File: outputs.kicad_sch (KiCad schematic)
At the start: 28 parts, among them J5 LED0123, J7 3.3V, M1 Motor_DC, U10 DRV2605LDGS, U21 WM8960, U9 PLP5012PWR

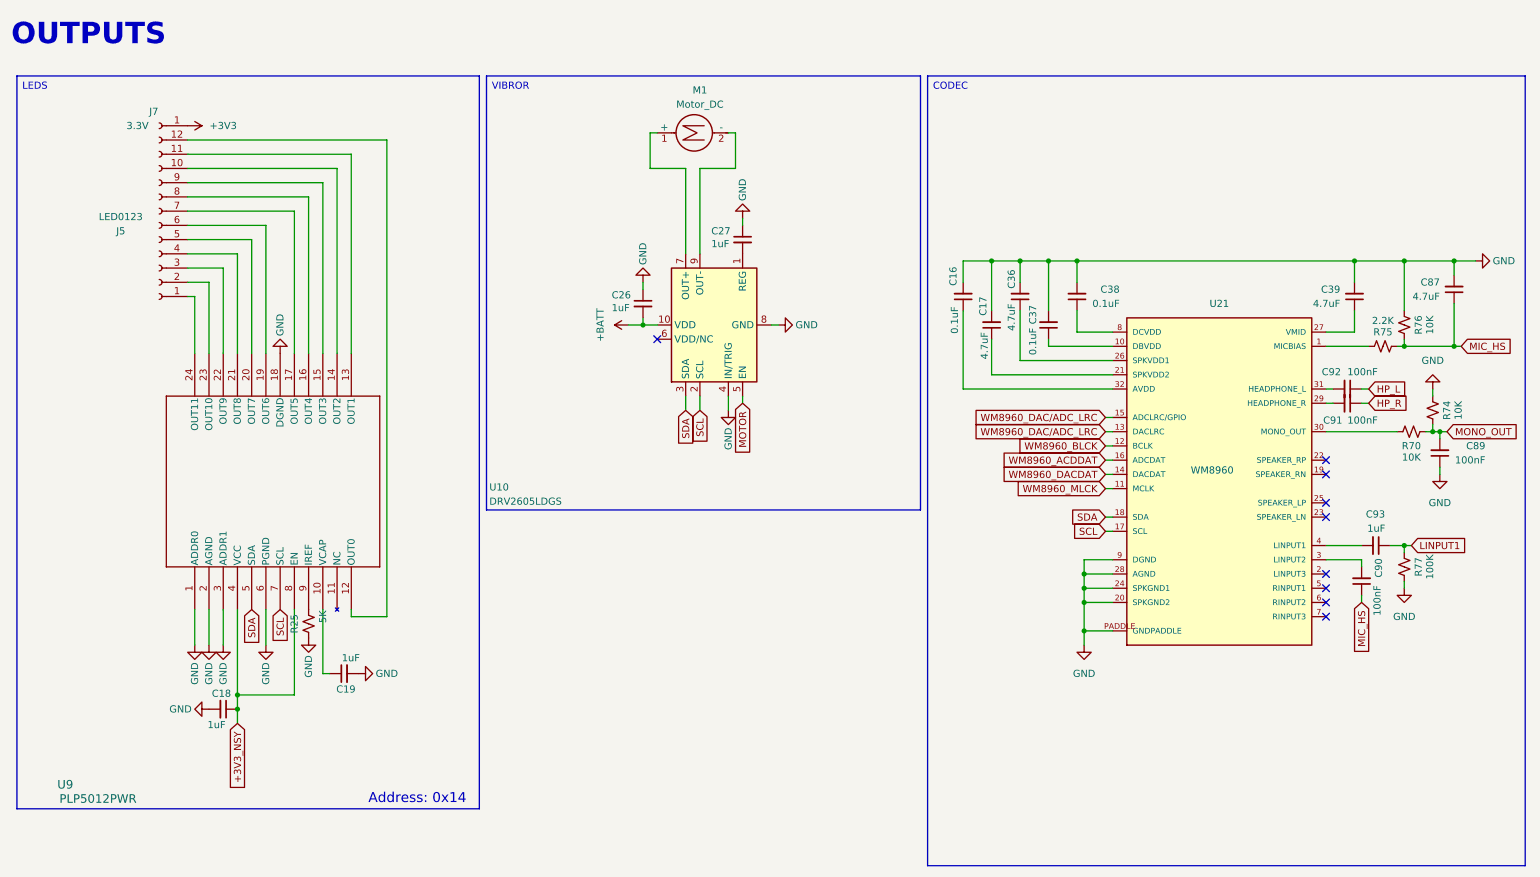
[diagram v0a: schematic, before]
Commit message: Routed RF Core
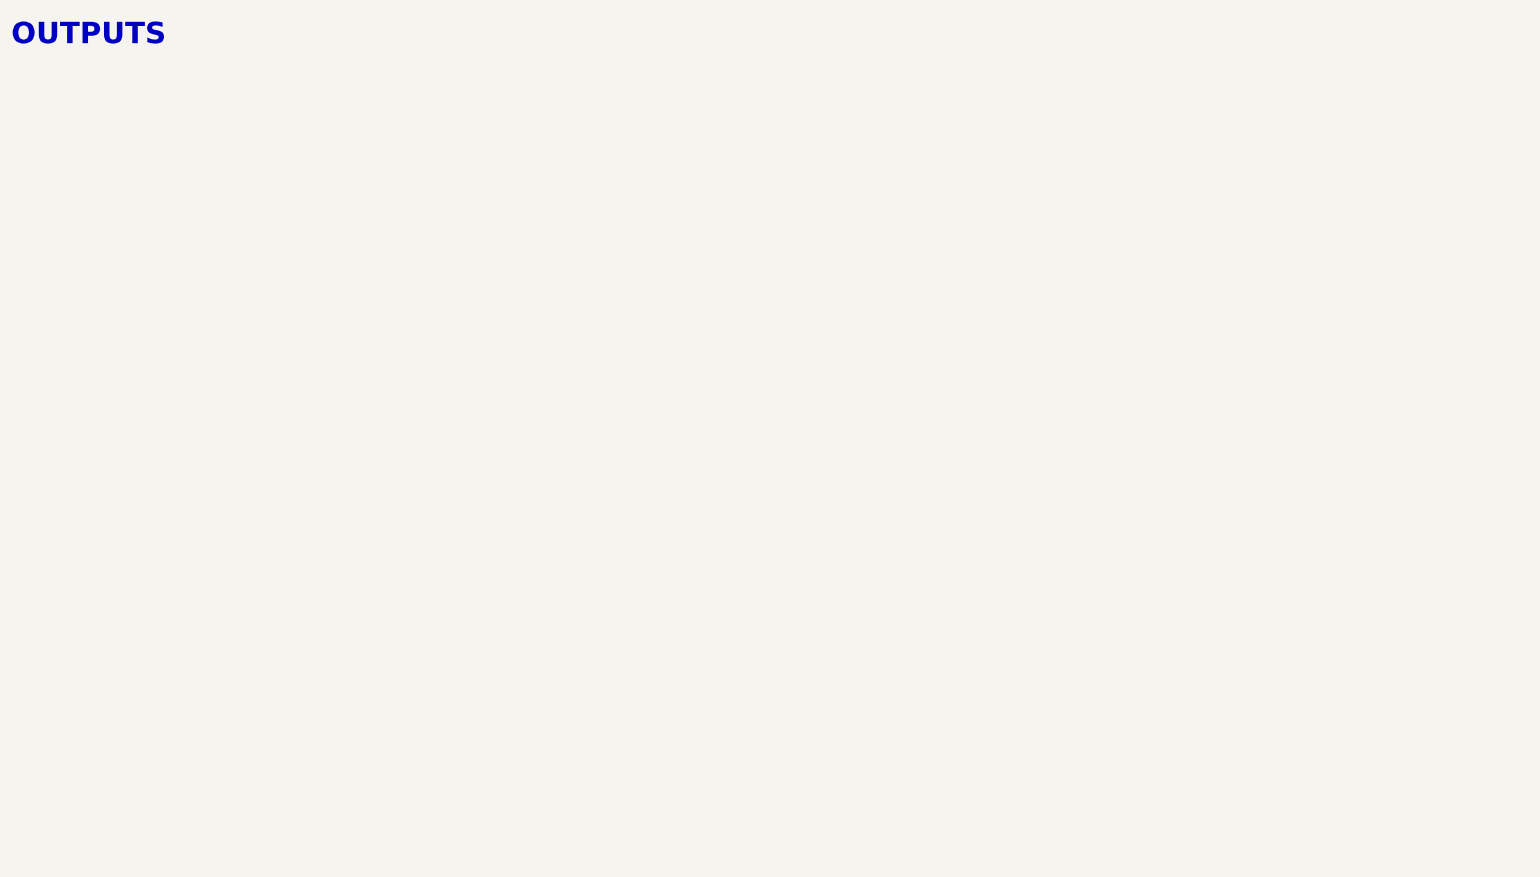
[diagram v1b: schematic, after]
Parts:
- removed C16, C37, C38: 0.1uF, Capacitor_SMD:C_0603_1608Metric, symbol Device:C_Small
- removed C17, C36, C39, C87: 4.7uF, Capacitor_SMD:C_0603_1608Metric, symbol Device:C_Small
- removed C18, C19, C26, C27, C93: 1uF, Capacitor_SMD:C_0603_1608Metric, symbol Device:C_Small
- removed C89, C90, C91, C92: 100nF, Capacitor_SMD:C_0603_1608Metric, symbol Device:C_Small
- removed J5: LED0123, Connector_PinHeader_1.27mm:PinHeader_2x06_P1.27mm_Vertical, symbol Connector:Conn_01x12_Socket
- removed J7: 3.3V, Connector_PinHeader_1.27mm:PinHeader_1x01_P1.27mm_Vertical, symbol Connector:Conn_01x01_Socket
- removed M1: Motor_DC, Connector_PinHeader_1.27mm:PinHeader_1x02_P1.27mm_Vertical, symbol Motor:Motor_DC
- removed R25: 5K, Resistor_SMD:R_0603_1608Metric, symbol Device:R_Small_US
- removed R70, R74, R76: 10K, Resistor_SMD:R_0603_1608Metric, symbol Device:R_Small_US
- removed R75: 2.2K, Resistor_SMD:R_0603_1608Metric, symbol Device:R_Small_US
- removed R77: 100K, Resistor_SMD:R_0603_1608Metric, symbol Device:R_Small_US
- removed U10: DRV2605LDGS, Package_SO:TSSOP-10_3x3mm_P0.5mm, symbol Driver:DRV2605LDGS
- removed U21: WM8960, PTCR:QFN-32, symbol PTCR-V5:WM8960
- removed U9: PLP5012PWR, PTCR:TSSOP24_PW_TEX, symbol LoRa-Phone:PLP5012PWR
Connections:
- no-connect marks 9 -> 0
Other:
- note removed: "Address: 0x14"
